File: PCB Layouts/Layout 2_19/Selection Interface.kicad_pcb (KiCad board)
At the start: 4 copper layers, 107.5 x 80 mm, 97 parts, among them J1 Conn_01x02

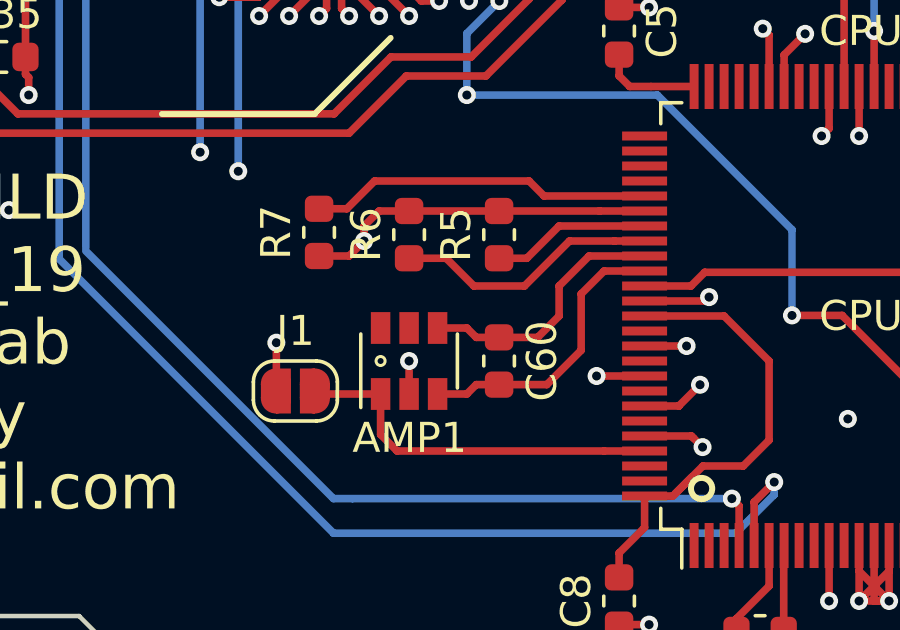
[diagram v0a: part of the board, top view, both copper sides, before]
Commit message: Decided to make connection between TIA_R_Common and op-amp Vout permanent to reduce solder complexity and because that pin cannot be routed by the PSoC anyway
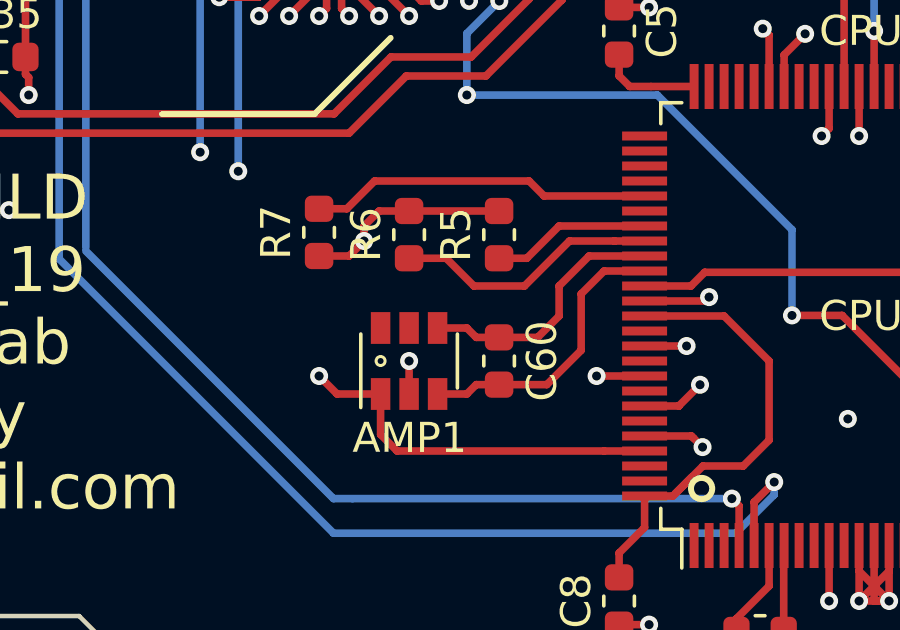
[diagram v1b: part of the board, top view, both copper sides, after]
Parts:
- removed J1: Conn_01x02, Jumper:SolderJumper-2_P1.3mm_Open_RoundedPad1.0x1.5mm
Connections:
- CPU1 pad 81: TIA_R_COMMON -> Net-(CPU1-Pad81)
- R5 pad 2: TIA_R_COMMON -> AMP1_VOUT
- R6 pad 2: TIA_R_COMMON -> AMP1_VOUT
- R7 pad 2: TIA_R_COMMON -> AMP1_VOUT
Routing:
- net TIA_R_COMMON: track 18.0 -> 0.00 mm, vias 2 -> 0
- net AMP1_VOUT: track 12.6 -> 24.7 mm, vias 0 -> 2

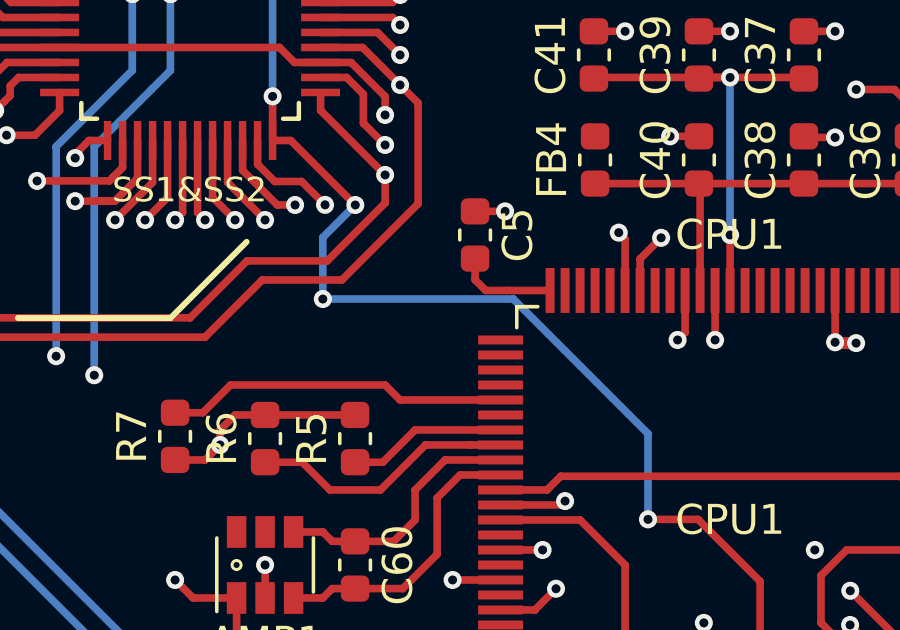
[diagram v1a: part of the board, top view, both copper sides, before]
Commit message: Added physical SAR bypass capacitor to Layout 2_19
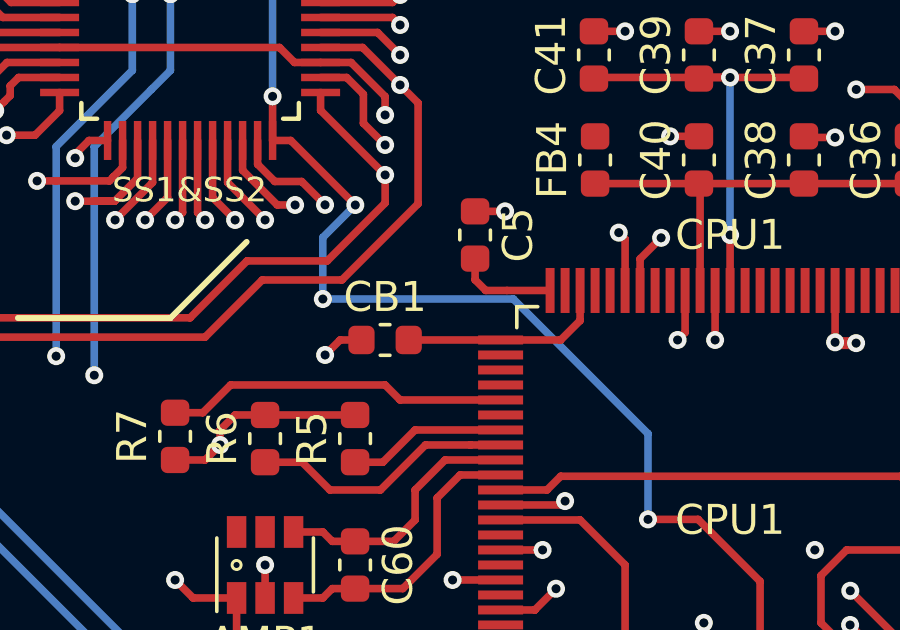
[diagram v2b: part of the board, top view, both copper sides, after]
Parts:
- added CB1: 1uF, Capacitor_SMD:C_0603_1608Metric, F.Cu at (227.5, 129.0)
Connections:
- net Net-(CPU1-Pad74) renamed DeltaSigma_Bypass_Cap
- CPU1 pad 73: Net-(CPU1-Pad73) -> SAR1_Bypass_Cap
- CPU1 pad 76: Net-(CPU1-Pad76) -> SAR1_Bypass_Cap
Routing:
- net SAR1_Bypass_Cap: track 0.00 -> 6.98 mm
- net GND: track 430.5 -> 431.9 mm, vias 153 -> 154

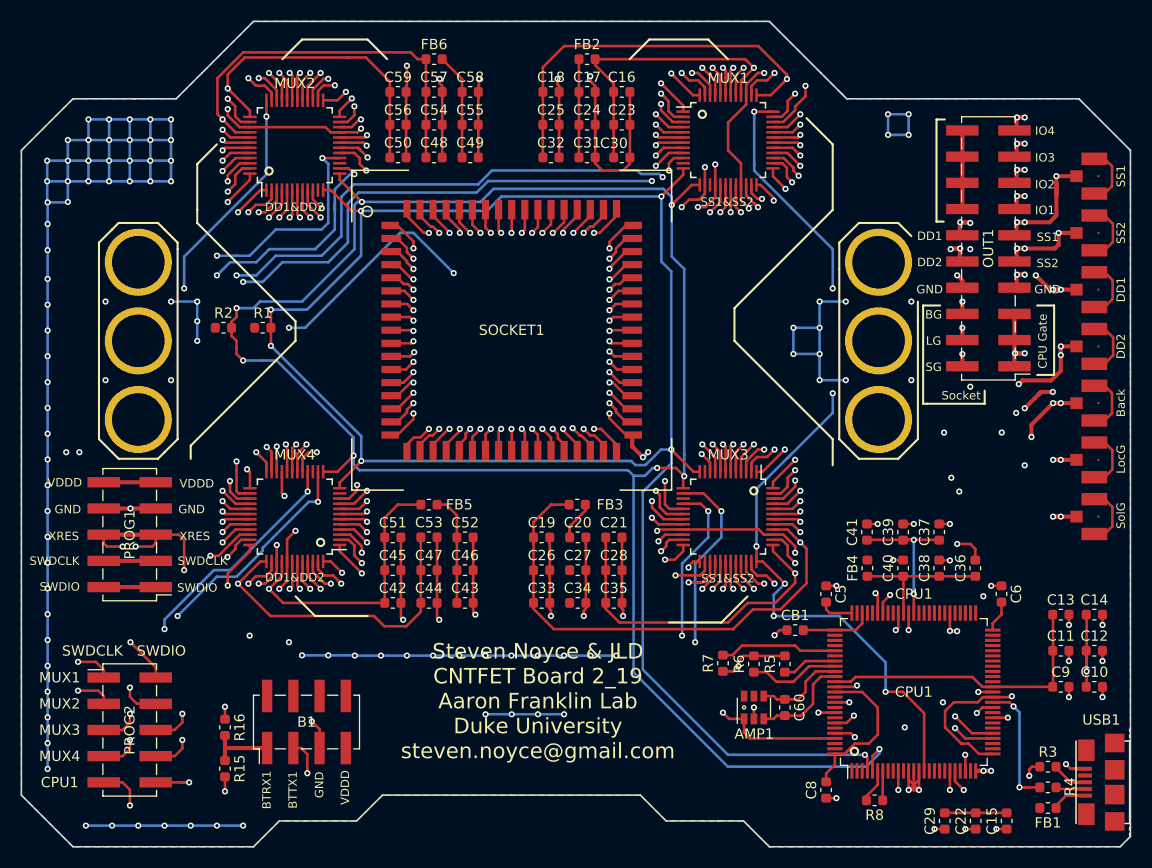
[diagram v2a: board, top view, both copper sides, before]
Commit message: Added a bypass capacitor for the delta-sigma ADC. Slightly improved the copper pours on a few layers
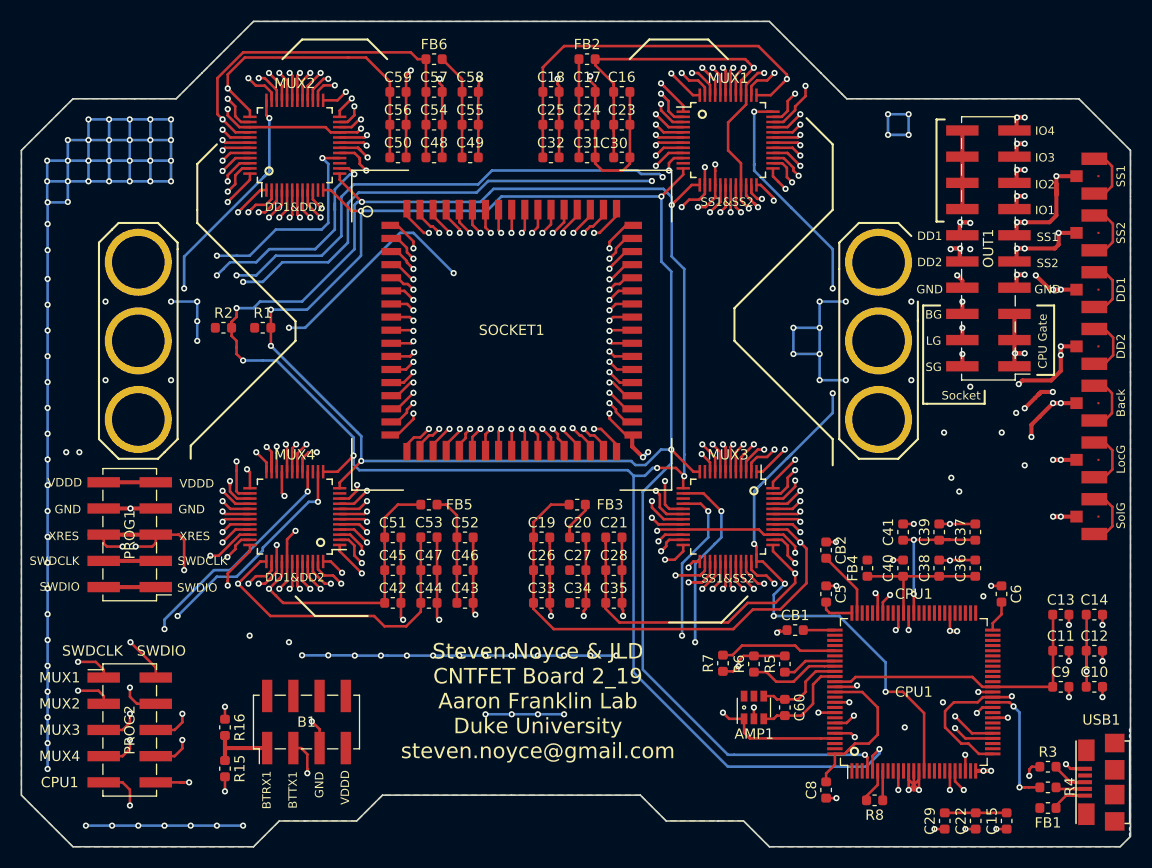
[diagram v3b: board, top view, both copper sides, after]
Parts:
- added CB2: 1uF, Capacitor_SMD:C_0603_1608Metric, F.Cu at (230.5, 121.2)
- moved C37 3.50 mm to (245.0, 119.5)
- moved C39 3.50 mm to (241.5, 119.5)
- moved C41 3.50 mm to (238.0, 119.5)
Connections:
- CPU1 pad 73: SAR1_Bypass_Cap -> SAR2_Bypass_Cap
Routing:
- net DeltaSigma_Bypass_Cap: track 0.00 -> 6.56 mm
- net SAR1_Bypass_Cap: track 6.98 -> 3.06 mm
- net GND: track 431.9 -> 434.4 mm, vias 154 -> 153
- net DD1: track 245.0 -> 242.8 mm
- net XRES: track 218.6 -> 219.9 mm
- net DD2: track 238.2 -> 237.0 mm

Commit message: Removed unused SMD capacitors from Layout 2_19
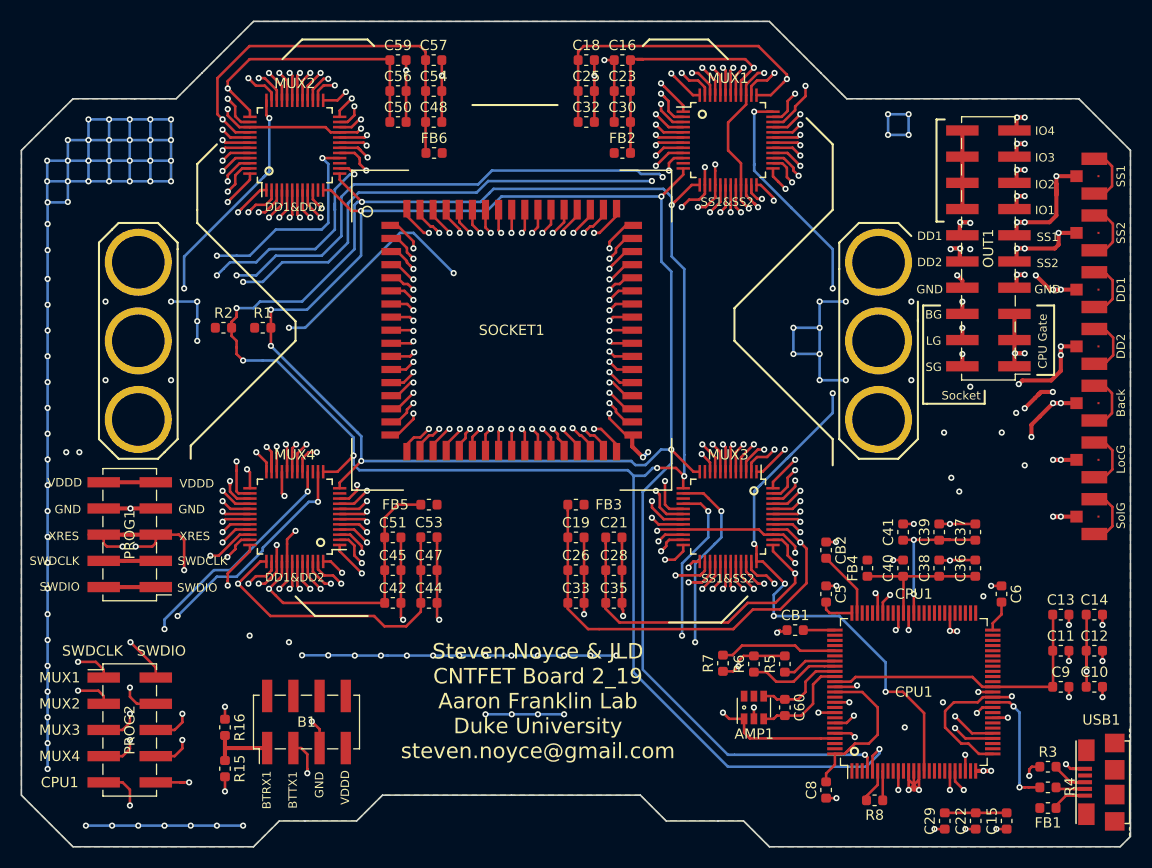
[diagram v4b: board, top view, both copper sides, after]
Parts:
- removed C17, C20, C43, C49: 47uF, Capacitor_SMD:C_0603_1608Metric
- removed C24, C27, C46, C55: 1uF, Capacitor_SMD:C_0603_1608Metric
- removed C31, C34, C52, C58: 0.1uF, Capacitor_SMD:C_0603_1608Metric
- moved FB2 9.71 mm to (210.8, 82.8)
- moved FB6 9.09 mm to (192.5, 82.8)
- moved C32 4.85 mm to (207.2, 79.8)
- moved C25 4.72 mm to (207.2, 76.8)
- moved C18 4.60 mm to (207.2, 73.8)
- moved C30 3.44 mm to (210.8, 79.8), turned to 180 degrees
- moved C48 3.44 mm to (192.5, 79.8)
- moved C50 3.44 mm to (189.0, 79.8)
- moved C19 3.32 mm to (206.2, 120.0)
- moved C26 3.32 mm to (206.2, 123.2)
- moved C33 3.32 mm to (206.2, 126.4)
- moved C23 3.26 mm to (210.8, 76.8), turned to 180 degrees
- moved C54 3.26 mm to (192.5, 76.8)
- moved C56 3.26 mm to (189.0, 76.8)
- moved C16 3.09 mm to (210.8, 73.8), turned to 180 degrees
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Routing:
- net GND: track 434.4 -> 391.5 mm, vias 153 -> 150
- net VDDD: track 165.8 -> 130.8 mm
- net VCCD_M1: track 38.4 -> 32.4 mm
- net VDDA_M3: track 49.0 -> 43.3 mm
- net VDDA_M1: track 29.4 -> 25.1 mm
- net VCCD_M2: track 29.8 -> 27.0 mm

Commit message: In Layout 2_19, heavily cleaned up routing from MUXes to the package to follow a standard pitch guideline. Cleaned up silkscreen. Renamed some SMD components to improve clarity.
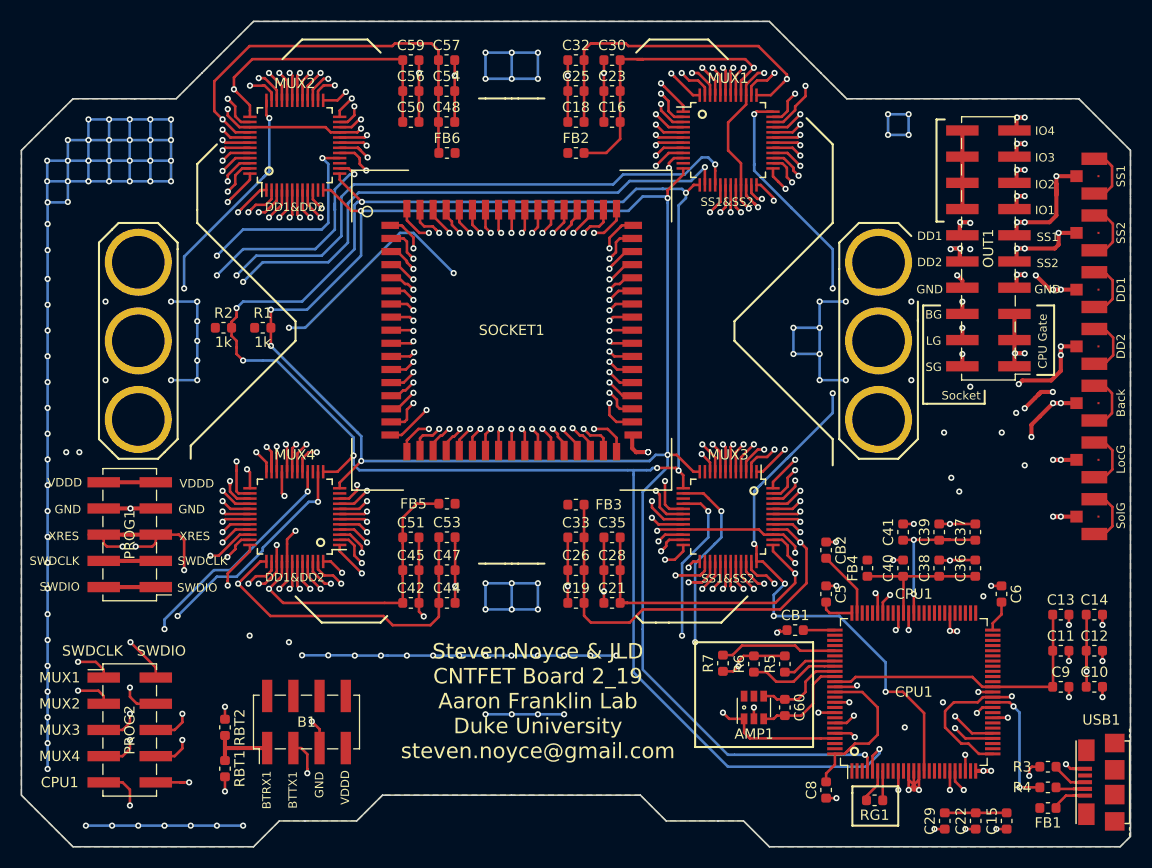
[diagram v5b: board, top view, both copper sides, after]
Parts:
- removed R15: 1k, Resistor_SMD:R_0603_1608Metric
- removed R16: 2k, Resistor_SMD:R_0603_1608Metric
- removed R8: 1M, Resistor_SMD:R_0603_1608Metric
- added RBT1: 1k, Resistor_SMD:R_0603_1608Metric, F.Cu at (172.2, 142.4)
- added RBT2: 2k, Resistor_SMD:R_0603_1608Metric, F.Cu at (172.2, 138.4)
- added RG1: 1M, Resistor_SMD:R_0603_1608Metric, F.Cu at (235.2, 145.5)
- moved C21 6.35 mm to (209.8, 126.4), turned to 180 degrees
- moved C35 6.35 mm to (209.8, 120.0), turned to 180 degrees
- moved C19 6.35 mm to (206.2, 126.4), turned to 180 degrees
- moved C33 6.35 mm to (206.2, 120.0), turned to 180 degrees
- moved C16 6.08 mm to (209.8, 79.8)
- moved C18 6.08 mm to (206.2, 79.8), turned to 180 degrees
- moved C30 6.08 mm to (209.8, 73.8)
- moved C32 6.08 mm to (206.2, 73.8), turned to 180 degrees
- moved FB2 4.50 mm to (206.2, 82.8)
- moved FB5 1.75 mm to (193.8, 116.8)
- moved C42 1.75 mm to (190.2, 126.4)
- moved C44 1.75 mm to (193.8, 126.4)
- moved C45 1.75 mm to (190.2, 123.2)
- moved C47 1.75 mm to (193.8, 123.2)
- moved C51 1.75 mm to (190.2, 120.0)
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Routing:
- net GND: track 391.5 -> 429.0 mm, vias 150 -> 164
- net D18: track 54.2 -> 48.8 mm
- net D20: track 55.3 -> 51.3 mm
- net VDDA_M1: track 25.1 -> 28.8 mm
- net BackGate_Socket: track 74.2 -> 70.5 mm, vias 7 -> 6
- net VCCD_M3: track 32.0 -> 29.2 mm
- net D22: track 59.5 -> 56.7 mm
- net D19: track 52.3 -> 49.6 mm
- net SWDIO1: track 121.0 -> 118.7 mm, vias 5 -> 3
- net D54: track 58.4 -> 56.1 mm
- net SWDCLK1: track 122.1 -> 119.8 mm, vias 6 -> 4
- net VCCD_M4: track 30.9 -> 32.8 mm
- net VDDA_M4: track 27.2 -> 29.0 mm
- net VDDA_M2: track 38.9 -> 40.7 mm
- net VDDA_M3: track 43.3 -> 41.6 mm
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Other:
- board text added: "1k"
